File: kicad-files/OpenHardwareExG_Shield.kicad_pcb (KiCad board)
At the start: 4 copper layers, 125.1 x 59.7 mm, 200 parts, among them P1 CONN_1, P10 CONN_18, P11 CONN_1, P12 CONN_1, P13 CONN_1, P14 CONN_1, P15 CONN_1, P16 CONN_1, P17 CONN_1, P18 CONN_1, P19 ARDUINO_SHIELD, P2 CONN_1, P20 CONN_3X2, P21 CONN_3X2, P22 CONN_7, P23 CONN_1, P24 CONN_1, P25 CONN_1, P26 CONN_1, P27 CONN_1, P28 CONN_1, P29 CONN_1, P3 CONN_1, P30 CONN_1, P31 CONN_1, P32 CONN_1, P33 CONN_1, P34 CONN_1, P35 CONN_1, P36 CONN_1, P37 CONN_1, P38 CONN_1, P39 CONN_1, P4 CONN_1, P40 CONN_1, P41 CONN_1, P42 CONN_1, P43 CONN_1, P44 CONN_1, P45 CONN_1, P46 CONN_1, P47 CONN_1, P48 CONN_1, P49 CONN_1, P5 CONN_1, P50 CONN_1, P51 CONN_1, P52 CONN_1, P53 CONN_1, P54 CONN_1, P55 CONN_1, P6 CONN_1, P7 CONN_1, P8 CONN_1, P9 CONN_1, U1 ADS1299, U2 Z0109MNT1G, U3 TL431BIDBZR, U4 873-AAT3220IGY-33T1, U5 ADUM6000, U6 SI8663, U7 74LS02, U8 74LS00, U9 74LS125

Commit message: pcb v0.2.1: fix text alignement of multi-line text
It seems that the switch to KiCAD v4 may have changed
the way multi-line text items are aligned on PCBs.

This converts all multi-line to multiple single line items.
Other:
- board text added: "Ace Medlock"
- board text added: "Eric Herman"
- board text added: "GPIO"
- board text added: "Kendrick Shaw"
- board text added: "Licensed under CERN OHL v.1.2 or later"
- board text added: "http://ohwr.org/cernohl"
- board text added: "rev. 0.2.1"
- board text removed: "Ace Medlock Eric Herman Kendrick Shaw"
- board text removed: "GPIO 1"
- board text removed: "GPIO 2"
- board text removed: "GPIO 3"
- board text removed: "GPIO 4"
- board text removed: "Licensed under CERN OHL v.1.2 or later http://ohwr.org/cernohl"
- board text removed: "_ +"
- board text removed: "rev. 0.2"
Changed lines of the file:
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@@
     (area 56.643704 27.7613 187.196296 91.5924)
     (thickness 1.6)
-    (drawings 67)
+    (drawings 84)
     (tracks 1168)
     (zones 0)
@@
   (page A3)
   (layers
-    (0 F.Cu signal)
-    (1 Inner2.Cu power)
-    (2 Inner1.Cu power)
-    (31 B.Cu signal)
-    (32 B.Adhes user)
-    (33 F.Adhes user)
-    (34 B.Paste user)
-    (35 F.Paste user)
+    (0 F.Cu signal hide)
+    (1 Inner2.Cu power hide)
+    (2 Inner1.Cu power hide)
+    (31 B.Cu signal hide)
+    (32 B.Adhes user hide)
+    (33 F.Adhes user hide)
+    (34 B.Paste user hide)
+    (35 F.Paste user hide)
     (36 B.SilkS user)
     (37 F.SilkS user)
-    (38 B.Mask user)
-    (39 F.Mask user)
-    (40 Dwgs.User user)
-    (41 Cmts.User user)
-    (42 Eco1.User user)
-    (43 Eco2.User user)
+    (38 B.Mask user hide)
+    (39 F.Mask user hide)
+    (40 Dwgs.User user hide)
+    (41 Cmts.User user hide)
+    (42 Eco1.User user hide)
+    (43 Eco2.User user hide)
     (44 Edge.Cuts user)
-    (46 B.CrtYd user)
-    (47 F.CrtYd user)
+    (46 B.CrtYd user hide)
+    (47 F.CrtYd user hide)
   )
   (setup
@@
     (mod_text_size 1 1)
     (mod_text_width 0.15)
-    (pad_size 1.00076 1.00076)
-    (pad_drill 0)
+    (pad_size 1.524 1.524)
+    (pad_drill 1.016)
     (pad_to_mask_clearance 0)
     (aux_axis_origin 0 0)
@@
       (solder_mask_margin 0.77) (clearance 0.77))
   )
-  (gr_text "GPIO\n1" (at 104.14 40.005) (layer F.SilkS)
+  (gr_text "Kendrick Shaw" (at 155.448 84.074) (layer F.SilkS)
+    (effects (font (size 1.016 1.016) (thickness 0.2032)))
+  )
+  (gr_text "Eric Herman" (at 155.448 82.804) (layer F.SilkS)
+    (effects (font (size 1.016 1.016) (thickness 0.2032)))
+  )
+  (gr_text "Ace Medlock" (at 155.448 81.28) (layer F.SilkS)
+    (effects (font (size 1.016 1.016) (thickness 0.2032)))
+  )
+  (gr_text http://ohwr.org/cernohl (at 99.314 87.63) (layer B.SilkS)
+    (effects (font (size 1.016 1.016) (thickness 0.2032)) (justify mirror))
+  )
+  (gr_text "Licensed under CERN OHL v.1.2 or later" (at 99.314 85.852) (layer F.SilkS)
+    (effects (font (size 1.016 1.016) (thickness 0.2032)))
+  )
+  (gr_text + (at 65.786 78.74) (layer F.SilkS)
+    (effects (font (size 1.016 1.5) (thickness 0.254)))
+  )
+  (gr_text + (at 65.786 73.66) (layer F.SilkS)
+    (effects (font (size 1.016 1.5) (thickness 0.254)))
+  )
+  (gr_text + (at 65.786 68.58) (layer F.SilkS)
+    (effects (font (size 1.016 1.5) (thickness 0.254)))
+  )
+  (gr_text + (at 65.786 63.5) (layer F.SilkS)
+    (effects (font (size 1.016 1.5) (thickness 0.254)))
+  )
+  (gr_text + (at 65.786 58.42) (layer F.SilkS)
+    (effects (font (size 1.016 1.5) (thickness 0.254)))
+  )
+  (gr_text + (at 65.786 53.34) (layer F.SilkS)
+    (effects (font (size 1.016 1.5) (thickness 0.254)))
+  )
+  (gr_text + (at 65.786 48.26) (layer F.SilkS)
+    (effects (font (size 1.016 1.5) (thickness 0.254)))
+  )
+  (gr_text http://ohwr.org/cernohl (at 99.314 87.63) (layer F.SilkS)
+    (effects (font (size 1.016 1.016) (thickness 0.2032)))
+  )
+  (gr_text "Kendrick Shaw" (at 155.321 84.074) (layer B.SilkS)
+    (effects (font (size 1.016 1.016) (thickness 0.2032)) (justify mirror))
+  )
+  (gr_text "Eric Herman" (at 155.321 82.677) (layer B.SilkS)
+    (effects (font (size 1.016 1.016) (thickness 0.2032)) (justify mirror))
+  )
+  (gr_text 1 (at 104.14 40.894) (layer F.SilkS)
+    (effects (font (size 0.5842 0.5842) (thickness 0.127)))
+  )
+  (gr_text 2 (at 101.6 40.894) (layer F.SilkS)
+    (effects (font (size 0.5842 0.5842) (thickness 0.127)))
+  )
+  (gr_text 3 (at 99.06 40.894) (layer F.SilkS)
+    (effects (font (size 0.5842 0.5842) (thickness 0.127)))
+  )
+  (gr_text 4 (at 96.52 40.894) (layer F.SilkS)
     (effects (font (size 0.5842 0.5842) (thickness 0.127)))
   )
-  (gr_text "GPIO\n2" (at 101.6 40.005) (layer F.SilkS)
+  (gr_text GPIO (at 104.14 40.005) (layer F.SilkS)
     (effects (font (size 0.5842 0.5842) (thickness 0.127)))
   )
-  (gr_text "GPIO\n3" (at 99.06 40.005) (layer F.SilkS)
+  (gr_text GPIO (at 101.6 40.005) (layer F.SilkS)
     (effects (font (size 0.5842 0.5842) (thickness 0.127)))
   )
-  (gr_text "GPIO\n4" (at 96.52 40.005) (layer F.SilkS)
+  (gr_text GPIO (at 99.06 40.005) (layer F.SilkS)
+    (effects (font (size 0.5842 0.5842) (thickness 0.127)))
+  )
+  (gr_text GPIO (at 96.52 40.005) (layer F.SilkS)
     (effects (font (size 0.5842 0.5842) (thickness 0.127)))
   )
@@
     (effects (font (size 1.016 1.016) (thickness 0.2032)) (justify mirror))
   )
-  (gr_text "rev. 0.2" (at 154.94 78.74) (layer F.SilkS)
+  (gr_text "rev. 0.2.1" (at 154.94 78.74) (layer F.SilkS)
     (effects (font (size 1.016 1.016) (thickness 0.2032)))
   )
-  (gr_text "rev. 0.2" (at 154.94 78.74) (layer B.SilkS)
-    (effects (font (size 1.016 1.016) (thickness 0.2032)) (justify mirror))
-  )
-  (gr_text "Licensed under CERN OHL v.1.2 or later\nhttp://ohwr.org/cernohl" (at 99.314 85.852) (layer B.SilkS)
+  (gr_text "rev. 0.2.1" (at 154.94 78.74) (layer B.SilkS)
     (effects (font (size 1.016 1.016) (thickness 0.2032)) (justify mirror))
   )
@@
     (effects (font (size 1.016 1.016) (thickness 0.2032)) (justify mirror))
   )
-  (gr_text "Ace Medlock\nEric Herman\nKendrick Shaw" (at 155.194 81.534) (layer B.SilkS)
-    (effects (font (size 1.016 1.016) (thickness 0.2032)) (justify mirror))
-  )
   (gr_text OpenHardwareExG_Shield (at 155.448 76.835) (layer B.SilkS)
     (effects (font (size 1.5 1.5) (thickness 0.3)) (justify mirror))
@@
     (effects (font (size 1.5 1.5) (thickness 0.3)) (justify mirror))
   )
-  (gr_text "Licensed under CERN OHL v.1.2 or later\nhttp://ohwr.org/cernohl" (at 99.314 85.852) (layer F.SilkS)
-    (effects (font (size 1.016 1.016) (thickness 0.2032)))
+  (gr_text "Licensed under CERN OHL v.1.2 or later" (at 99.314 85.852) (layer B.SilkS)
+    (effects (font (size 1.016 1.016) (thickness 0.2032)) (justify mirror))
   )
-  (gr_text "Ace Medlock\nEric Herman\nKendrick Shaw" (at 155.321 81.28) (layer F.SilkS)
-    (effects (font (size 1.016 1.016) (thickness 0.2032)))
+  (gr_text "Ace Medlock" (at 155.321 81.28) (layer B.SilkS)
+    (effects (font (size 1.016 1.016) (thickness 0.2032)) (justify mirror))
   )
   (gr_text OpenHardwareExG_Shield (at 155.448 76.835) (layer F.SilkS)
@@
     (effects (font (size 1.016 1.016) (thickness 0.2032)))
   )
-  (gr_text "_\n\n+" (at 65.786 70.612) (layer F.SilkS)
+  (gr_text - (at 65.786 71.12) (layer F.SilkS)
     (effects (font (size 1.016 1.5) (thickness 0.254)))
   )
-  (gr_text "_\n\n+" (at 65.786 75.692) (layer F.SilkS)
+  (gr_text - (at 65.786 76.2) (layer F.SilkS)
     (effects (font (size 1.016 1.5) (thickness 0.254)))
   )
-  (gr_text "_\n\n+" (at 65.786 60.452) (layer F.SilkS)
+  (gr_text - (at 65.786 60.96) (layer F.SilkS)
     (effects (font (size 1.016 1.5) (thickness 0.254)))
   )
-  (gr_text "_\n\n+" (at 65.786 55.372) (layer F.SilkS)
+  (gr_text - (at 65.786 55.88) (layer F.SilkS)
     (effects (font (size 1.016 1.5) (thickness 0.254)))
   )
-  (gr_text "_\n\n+" (at 65.786 50.292) (layer F.SilkS)
+  (gr_text - (at 65.786 50.8) (layer F.SilkS)
     (effects (font (size 1.016 1.5) (thickness 0.254)))
   )
-  (gr_text "_\n\n+" (at 65.786 45.212) (layer F.SilkS)
+  (gr_text - (at 65.786 45.72) (layer F.SilkS)
     (effects (font (size 1.016 1.5) (thickness 0.254)))
   )
-  (gr_text "_\n\n+" (at 65.786 65.532) (layer F.SilkS)
+  (gr_text - (at 65.786 66.04) (layer F.SilkS)
     (effects (font (size 1.016 1.5) (thickness 0.254)))
   )
-  (gr_text + (at 65.786 43.688) (layer F.SilkS)
+  (gr_text + (at 65.786 43.18) (layer F.SilkS)
     (effects (font (size 1.016 1.5) (thickness 0.254)))
   )
@@
   )
   (gr_text 1 (at 65.786 77.47) (layer F.SilkS)
-    (effects (font (size 1.5 1.5) (thickness 0.3)))
+    (effects (font (size 1.27 1.27) (thickness 0.3)))
   )
   (gr_text 2 (at 65.786 72.39) (layer F.SilkS)
-    (effects (font (size 1.27 1.5) (thickness 0.3)))
+    (effects (font (size 1.27 1.27) (thickness 0.3)))
   )
   (gr_text 3 (at 65.786 67.31) (layer F.SilkS)
-    (effects (font (size 1.27 1.5) (thickness 0.3)))
+    (effects (font (size 1.27 1.27) (thickness 0.3)))
   )
-  (gr_text 4 (at 65.786 62.484) (layer F.SilkS)
-    (effects (font (size 1.5 1.5) (thickness 0.3)))
+  (gr_text 4 (at 65.786 62.23) (layer F.SilkS)
+    (effects (font (size 1.27 1.27) (thickness 0.3)))
   )
   (gr_text 5 (at 65.786 57.15) (layer F.SilkS)
-    (effects (font (size 1.27 1.5) (thickness 0.3)))
+    (effects (font (size 1.27 1.27) (thickness 0.3)))
   )
-  (gr_text 6 (at 65.786 52.324) (layer F.SilkS)
-    (effects (font (size 1.27 1.5) (thickness 0.3)))
+  (gr_text 6 (at 65.786 52.07) (layer F.SilkS)
+    (effects (font (size 1.27 1.27) (thickness 0.3)))
   )
   (gr_text 7 (at 65.786 46.99) (layer F.SilkS)
-    (effects (font (size 1.27 1.5) (thickness 0.3)))
+    (effects (font (size 1.27 1.27) (thickness 0.3)))
   )
-  (gr_text 8 (at 65.786 42.164) (layer F.SilkS)
-    (effects (font (size 1.27 1.5) (thickness 0.3)))
+  (gr_text 8 (at 65.786 41.91) (layer F.SilkS)
+    (effects (font (size 1.27 1.27) (thickness 0.3)))
   )
   (gr_text RLD (at 63.5 35.56) (layer F.SilkS)

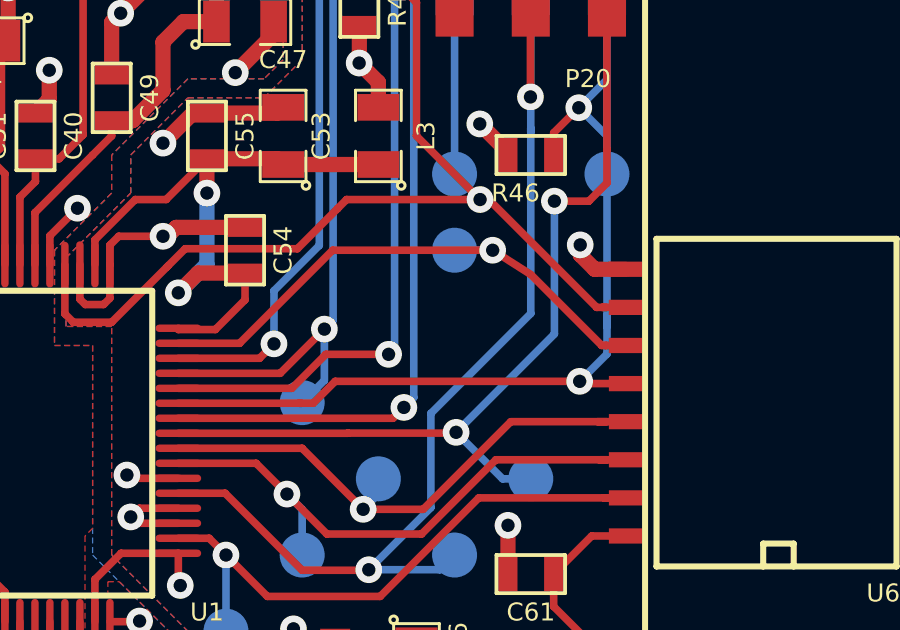
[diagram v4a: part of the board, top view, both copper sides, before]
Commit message: add pulldown resistors for GPIOs
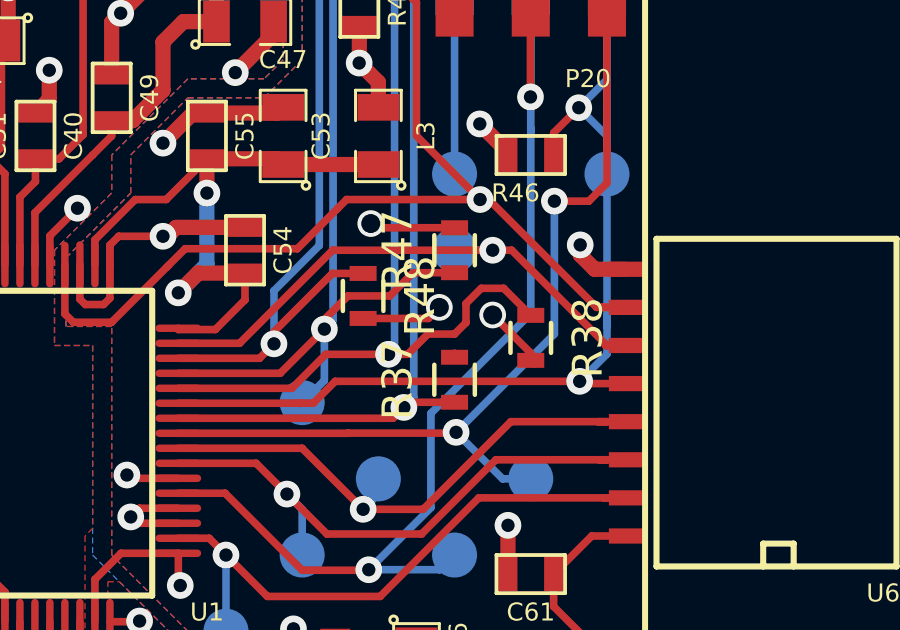
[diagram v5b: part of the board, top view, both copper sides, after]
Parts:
- added R37: 10k, Resistors_SMD:R_0603, F.Cu at (109.2, 57.7)
- added R38: 10k, Resistors_SMD:R_0603, F.Cu at (111.8, 56.3)
- added R47: 10k, Resistors_SMD:R_0603, F.Cu at (109.2, 53.3)
- added R48: 10k, Resistors_SMD:R_0603, F.Cu at (106.2, 54.9)
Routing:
- net AGND: track 162.5 -> 170.5 mm, vias 65 -> 68
- net /ADS129x_GPIO2_ISO: track 30.1 -> 36.5 mm
- net /ADS129x_GPIO3_ISO: track 31.1 -> 36.4 mm
- net /ADS129x_GPIO4_ISO: track 31.5 -> 35.7 mm
- net /ADS129x_GPIO1_ISO: track 31.5 -> 33.3 mm
- net /ADS129x_~DRDY~_ISO: track 18.7 -> 19.5 mm

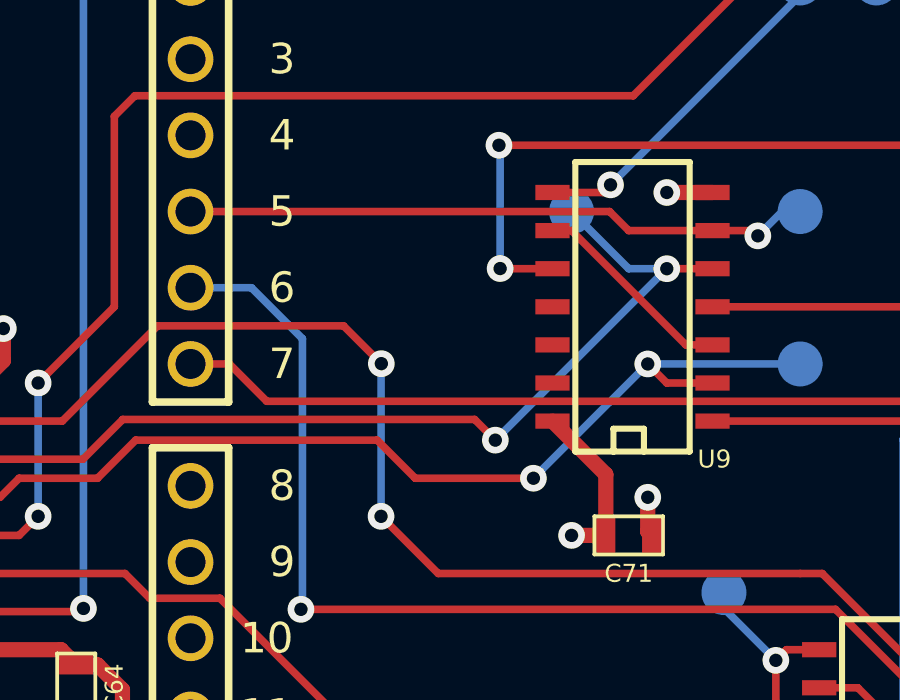
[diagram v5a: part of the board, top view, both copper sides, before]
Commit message: add label to Arduino header pins 5, 6, and 7
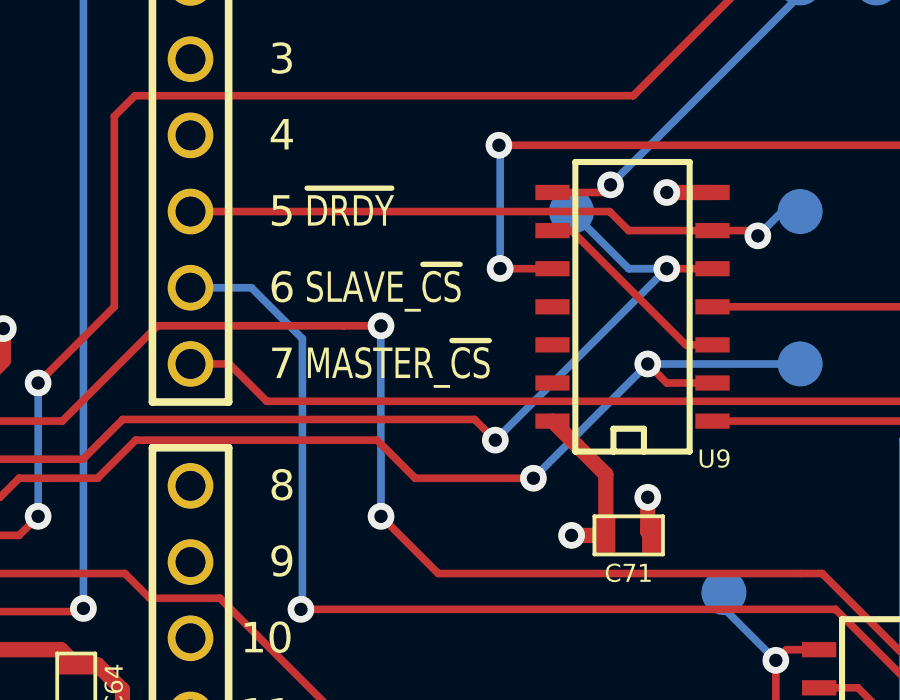
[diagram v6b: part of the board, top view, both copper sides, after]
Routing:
- net /MASTER: track 74.5 -> 75.2 mm
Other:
- board text added: "MASTER_~CS~"
- board text added: "SLAVE_~CS~"
- board text added: "~DRDY~"
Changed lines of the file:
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@@
     (links 383)
     (no_connects 0)
-    (area 59.004999 29.159999 184.200001 88.950001)
+    (area 56.718704 27.8883 187.121296 91.7448)
     (thickness 1.6)
-    (drawings 84)
-    (tracks 1197)
+    (drawings 87)
+    (tracks 1168)
     (zones 0)
     (modules 204)
@@
     (1 Inner2.Cu power hide)
     (2 Inner1.Cu power hide)
-    (31 B.Cu signal hide)
+    (31 B.Cu signal)
     (32 B.Adhes user hide)
     (33 F.Adhes user hide)
@@
     )
   )
+  (gr_text MASTER_~CS~ (at 135.89 53.34) (layer F.SilkS)
+    (effects (font (size 1.016 0.762) (thickness 0.1778)) (justify left))
+  )
+  (gr_text SLAVE_~CS~ (at 135.89 50.8) (layer F.SilkS)
+    (effects (font (size 1.016 0.762) (thickness 0.1778)) (justify left))
+  )
+  (gr_text ~DRDY~ (at 135.89 48.26) (layer F.SilkS)
+    (effects (font (size 1.016 0.762) (thickness 0.1778)) (justify left))
+  )
   (gr_text "Kendrick Shaw" (at 155.448 84.074) (layer F.SilkS)
     (effects (font (size 1.016 1.016) (thickness 0.2032)))
@@
   (segment (start 63.5 43.18) (end 68.58 43.18) (width 0.254) (layer B.Cu) (net 40))
   (segment (start 125.095 55.245) (end 127.805 55.245) (width 0.254) (layer F.Cu) (net 41))
-  (segment (start 137.18 52.07) (end 138.44 53.33) (width 0.254) (layer F.Cu) (net 41))
+  (segment (start 137.18 52.07) (end 138.43 52.07) (width 0.254) (layer F.Cu) (net 41))
   (segment (start 130.98 52.07) (end 137.18 52.07) (width 0.254) (layer F.Cu) (net 41))
   (segment (start 127.805 55.245) (end 130.98 52.07) (width 0.254) (layer F.Cu) (net 41))
@@
   (via (at 138.43 58.42) (size 0.889) (layers F.Cu B.Cu) (net 41))
   (segment (start 138.43 58.42) (end 140.335 60.325) (width 0.254) (layer F.Cu) (net 41))
-  (segment (start 138.43 58.42) (end 138.43 53.34) (width 0.254) (layer B.Cu) (net 41))
-  (segment (start 138.43 53.34) (end 138.44 53.33) (width 0.254) (layer B.Cu) (net 41))
-  (segment (start 138.43 53.34) (end 138.44 53.33) (width 0.254) (layer F.Cu) (net 41))
-  (via (at 138.44 53.33) (size 0.889) (layers F.Cu B.Cu) (net 41))
+  (segment (start 138.43 58.42) (end 138.42 52.08) (width 0.254) (layer B.Cu) (net 41))
+  (segment (start 138.42 52.08) (end 138.43 52.07) (width 0.254) (layer B.Cu) (net 41))
+  (segment (start 138.42 52.08) (end 138.43 52.07) (width 0.254) (layer F.Cu) (net 41))
+  (via (at 138.43 52.07) (size 0.889) (layers F.Cu B.Cu) (net 41))
   (via (at 151.59 63.22) (size 0.889) (layers F.Cu B.Cu) (net 42))
   (segment (start 149.86 60.96) (end 149.86 61.49) (width 0.254) (layer B.Cu) (net 42))
